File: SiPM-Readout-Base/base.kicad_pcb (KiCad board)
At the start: 2 copper layers, 90 x 90 mm, 94 parts

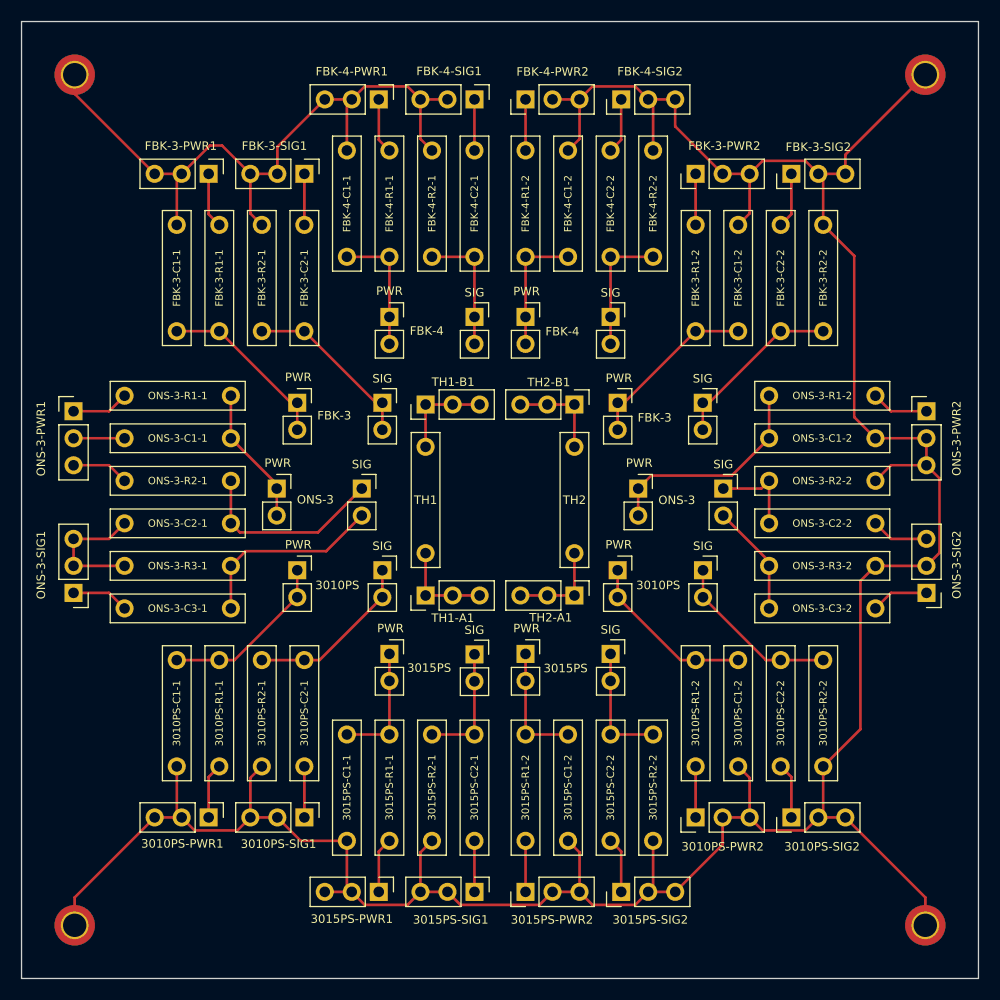
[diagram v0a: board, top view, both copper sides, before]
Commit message: Redesigned LED-Wide PCB; created Fabrication files; added template for fabrication order request; added final order contents.
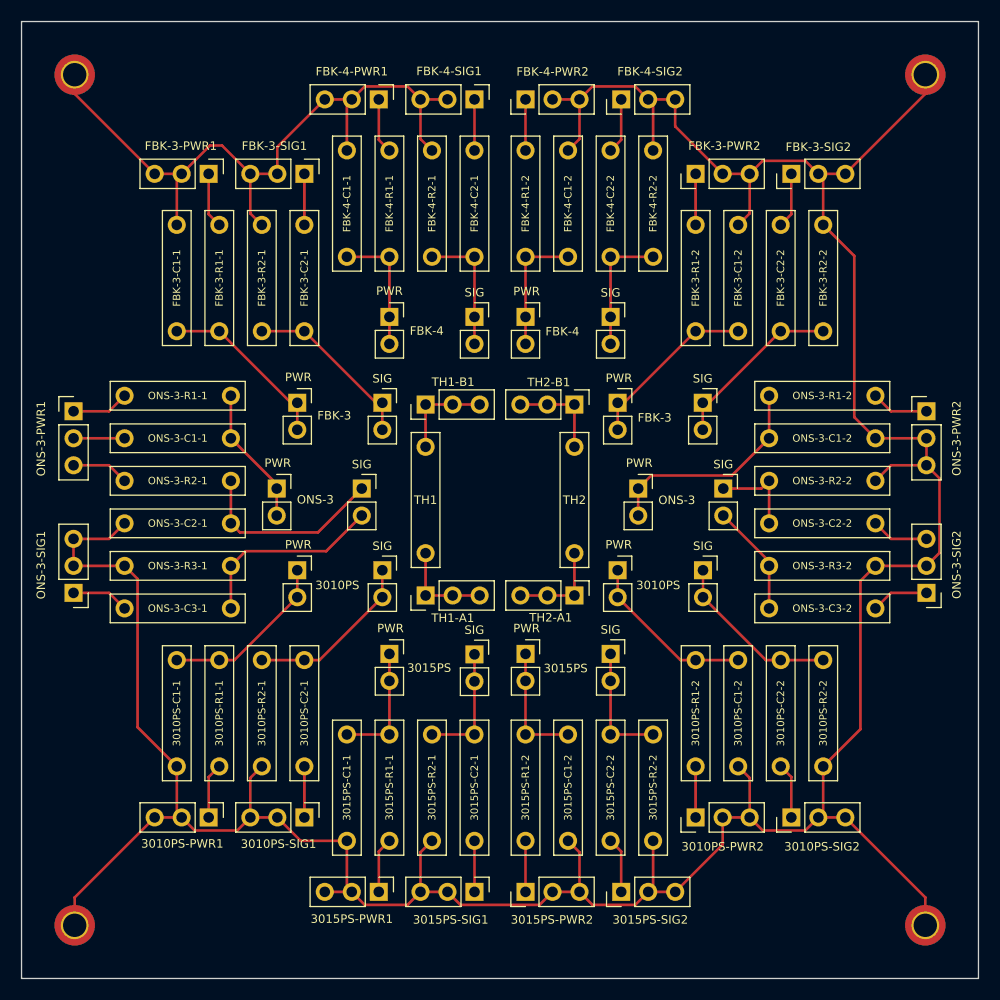
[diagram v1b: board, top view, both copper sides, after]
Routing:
- net GND: track 368.4 -> 389.3 mm
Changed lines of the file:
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@@
 			(drillshape 0)
 			(scaleselection 1)
-			(outputdirectory "outputs/")
+			(outputdirectory "Fabrication/")
 		)
 	)
@@
 	)
 	(segment
+		(start 118.5999 124.055)
+		(end 114.9159 120.371)
+		(width 0.25)
+		(layer "F.Cu")
+		(net 5)
+	)
+	(segment
 		(start 165.4799 63.865)
 		(end 165.4799 61.325)
@@
 	)
 	(segment
+		(start 188.9999 60.805)
+		(end 188.9999 59)
+		(width 0.25)
+		(layer "F.Cu")
+		(net 5)
+	)
+	(segment
 		(start 162.9399 61.325)
 		(end 165.4799 61.325)
@@
 	)
 	(segment
+		(start 114.9159 120.371)
+		(end 114.9159 106.421)
+		(width 0.25)
+		(layer "F.Cu")
+		(net 5)
+	)
+	(segment
 		(start 162.9399 61.325)
 		(end 161.7139 60.099)
@@
 	)
 	(segment
+		(start 114.9159 106.421)
+		(end 113.6899 105.195)
+		(width 0.25)
+		(layer "F.Cu")
+		(net 5)
+	)
+	(segment
 		(start 169.9399 131.395)
 		(end 169.9399 128.855)
@@
 	)
 	(segment
-		(start 188.9999 59)
-		(end 181.4799 66.52)
-		(width 0.25)
-		(layer "F.Cu")
-		(net 5)
-	)
-	(segment
 		(start 188.9999 136.375)
 		(end 181.4799 128.855)
@@
 	)
 	(segment
-		(start 181.4799 66.52)
-		(end 181.4799 68.325)
-		(width 0.25)
-		(layer "F.Cu")
-		(net 5)
-	)
-	(segment
 		(start 125.5199 68.325)
 		(end 122.8549 65.66)
@@
 		(width 0.25)
 		(layer "F.Cu")
+		(net 5)
+	)
+	(segment
+		(start 181.4799 68.325)
+		(end 188.9999 60.805)
+		(width 0.25)
+		(layer "F.Cu")
